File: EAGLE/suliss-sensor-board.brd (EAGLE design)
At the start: 77.5 x 60.6 mm, 29 parts, among them K1 61400826021, K2 61400826021, K3 61400826021, K4 61400826021, K5 61400826021, K6 61400826021, K7 61400826021, K8 61400826021, U1 PCF8574ADW, U2 LOLIN_NODEMCUV3

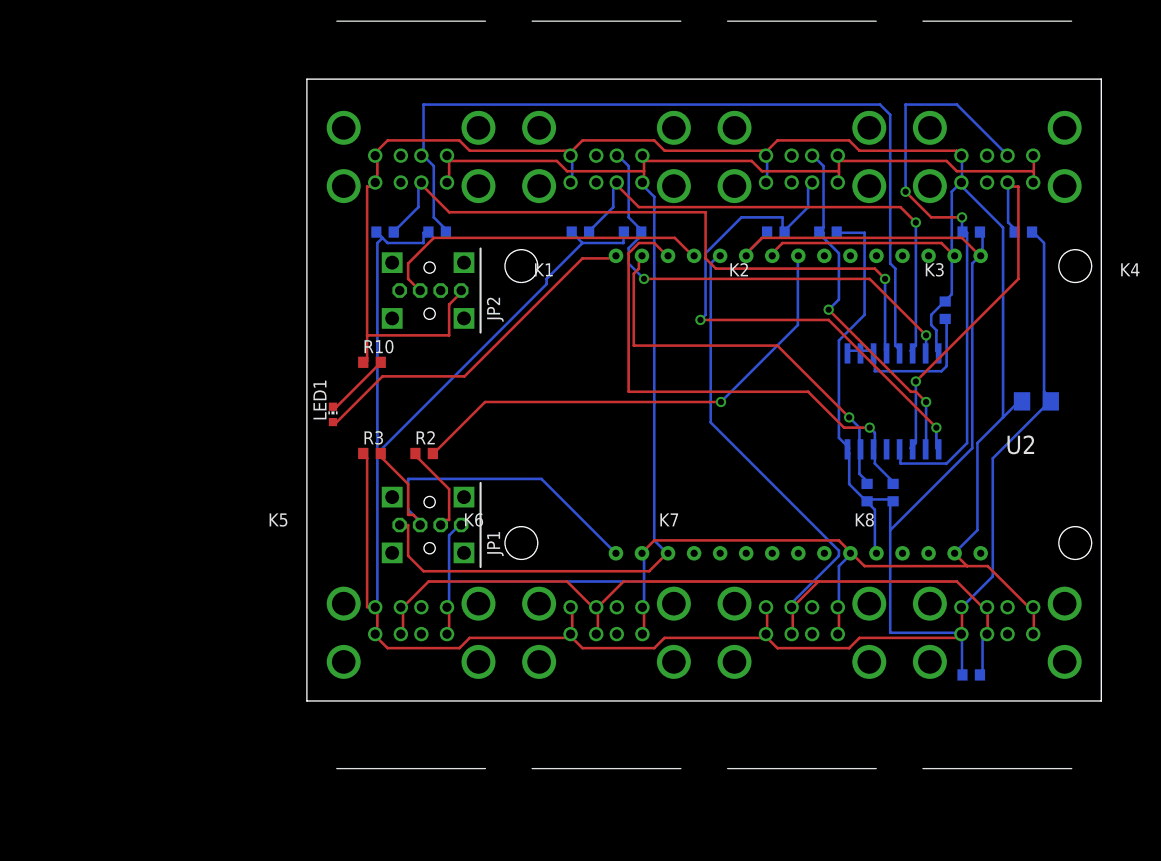
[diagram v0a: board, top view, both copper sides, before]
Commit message: Updated board with 3 holes
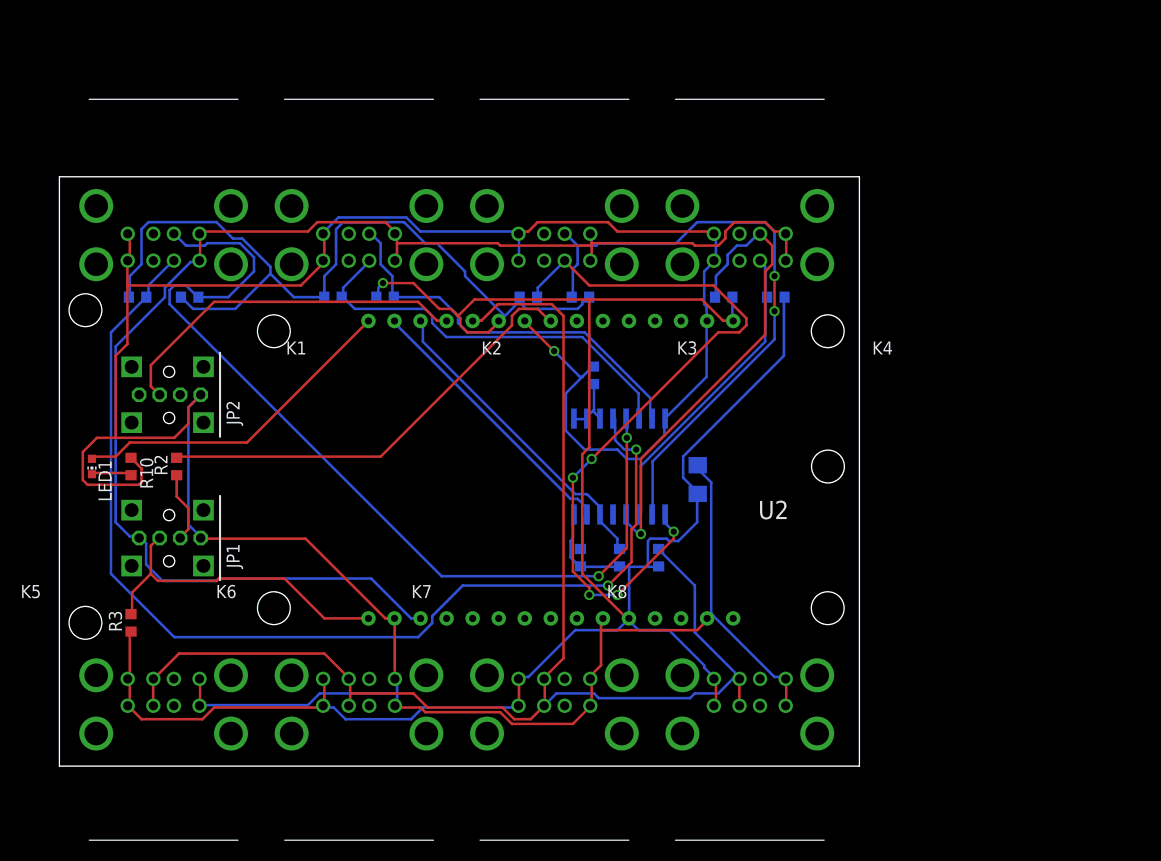
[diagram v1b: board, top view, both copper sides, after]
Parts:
- moved R4 34.9 mm to (52.1, 38.1)
- moved C1 33.9 mm to (62.2, 27.9), turned to 90 degrees
- moved R17 32.6 mm to (58.4, 20.3), turned to 270 degrees
- moved R3 28.7 mm to (6.99, 14.0), turned to 90 degrees
- moved R5 28.7 mm to (50.8, 20.3)
- moved R1 27.4 mm to (54.6, 20.3)
- moved U1 27.4 mm to (54.6, 29.2)
- moved JP2 27.4 mm to (10.8, 36.2)
- moved R10 25.6 mm to (6.99, 29.2), turned to 270 degrees
- moved JP1 25.4 mm to (10.8, 22.2)
- moved K2 25.3 mm to (29.2, 54.6)
- moved K3 25.3 mm to (48.3, 54.6)
- moved K1 25.3 mm to (10.2, 54.6)
- moved K4 25.3 mm to (67.3, 54.6)
- moved K6 25.1 mm to (29.2, 3.17)
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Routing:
- net !F0: track 65.0 -> 105.8 mm, vias 1 -> 2
- net 3.3V: track 330.6 -> 292.8 mm, vias 0 -> 1
- net !F5: track 34.9 -> 60.1 mm
- net GND: track 276.5 -> 300.6 mm, vias 0 -> 1
- net !F4: track 52.6 -> 73.8 mm, vias 2 -> 5
- net SCL: track 49.7 -> 31.0 mm, vias 1 -> 0
- net TMP: track 121.9 -> 135.3 mm
- net !F7: track 58.2 -> 46.4 mm, vias 2 -> 1
- net N$1: track 17.0 -> 6.08 mm
- net !F2: track 49.8 -> 40.3 mm, vias 1 -> 0
- net SDA: track 40.2 -> 30.7 mm, vias 1 -> 0
- net !F1: track 83.1 -> 91.0 mm, vias 0 -> 2
- net !F3: track 45.8 -> 38.9 mm, vias 2 -> 0
- net !F6: track 36.5 -> 30.2 mm, vias 1 -> 0
- net R_VALUE: track 37.0 -> 31.9 mm
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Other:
- board size 77.5 x 60.6 mm -> 78 x 57.5 mm
